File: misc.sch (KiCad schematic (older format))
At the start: 25 parts, among them CN8 POWER_INPUT, CN9 LED_CONNECTOR, SW1 POWER_SWITCH, SW2 RESET_SW, U10 NE555P, U11 74LS125, U12 74LS02, U9 74LS06

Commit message: Add buffers on joystick ports - WIP
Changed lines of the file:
@@
 Text Notes 6020 1880 0    50   ~ 0
 TCK-141
+$Comp
+L power:PWR_FLAG #FLG0103
+U 1 1 62290C11
+P 7000 1845
+F 0 "#FLG0103" H 7000 1920 50  0001 C CNN
+F 1 "PWR_FLAG" H 7000 2018 50  0000 C CNN
+F 2 "" H 7000 1845 50  0001 C CNN
+F 3 "~" H 7000 1845 50  0001 C CNN
+	1    7000 1845
+	1    0    0    -1
+$EndComp
+Wire Wire Line
+	7000 1845 7000 1945
 $EndSCHEMATC

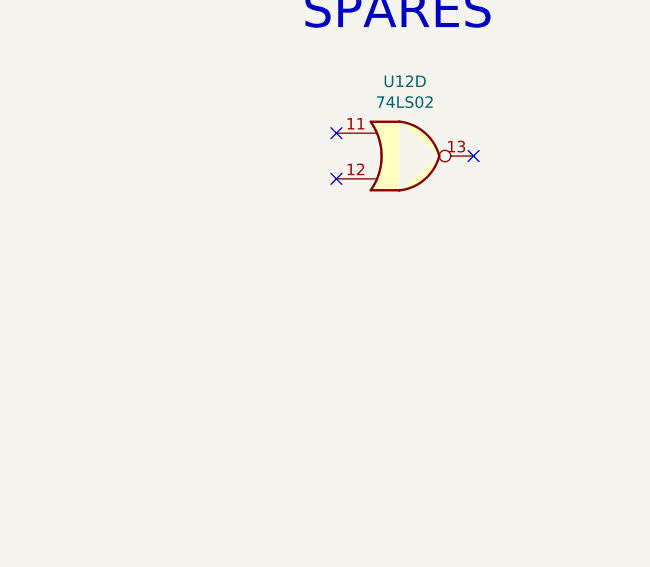
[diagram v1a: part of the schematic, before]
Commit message: Fit alt socket for 6510 Still some fine work TBD
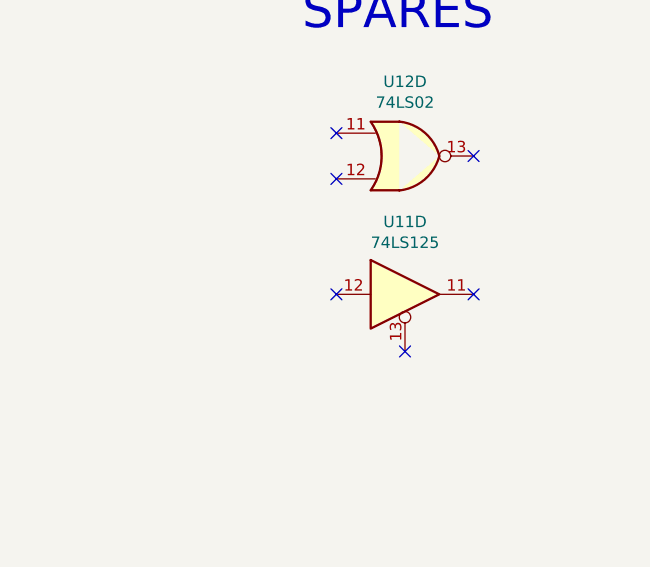
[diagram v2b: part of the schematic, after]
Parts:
- added unit 4 of U11
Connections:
- no-connect marks 5 -> 8
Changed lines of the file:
@@
 Wire Wire Line
 	7000 1845 7000 1945
+$Comp
+L 74xx:74LS125 U?
+U 4 1 625FE5B6
+P 9860 5960
+AR Path="/5ECB474B/625FE5B6" Ref="U?"  Part="4"
+AR Path="/5EACE220/625FE5B6" Ref="U11"  Part="4"
+F 0 "U11" H 9860 6277 50  0000 C CNN
+F 1 "74LS125" H 9860 6186 50  0000 C CNN
+F 2 "Package_DIP:DIP-14_W7.62mm_Socket_LongPads" H 9860 5960 50  0001 C CNN
+F 3 "http://www.ti.com/lit/gpn/sn74LS125" H 9860 5960 50  0001 C CNN
+	4    9860 5960
+	1    0    0    -1
+$EndComp
+NoConn ~ 9560 5960
+NoConn ~ 9860 6210
+NoConn ~ 10160 5960
 $EndSCHEMATC

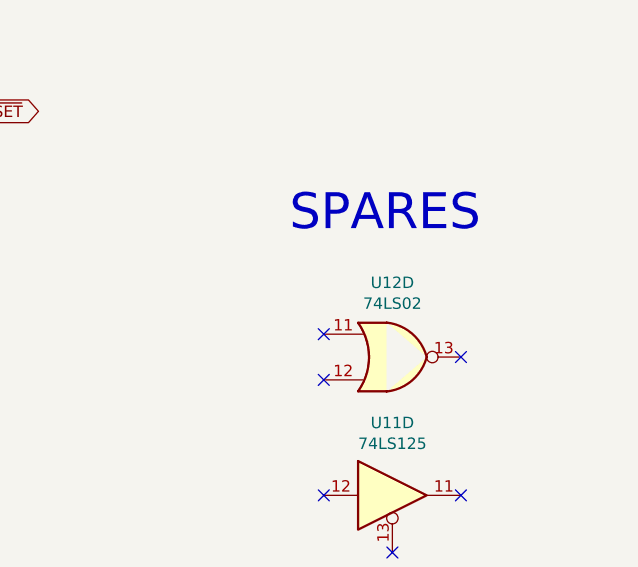
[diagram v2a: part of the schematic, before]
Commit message: Add a way to disable internal RAM from expansion connector
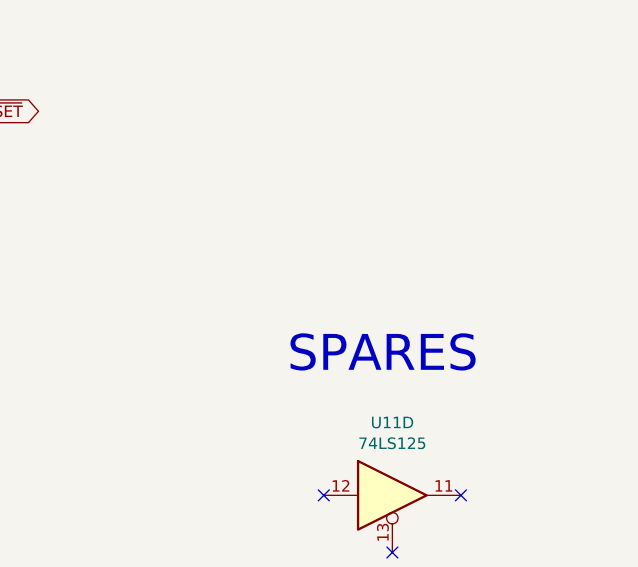
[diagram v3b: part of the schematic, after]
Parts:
- removed U12: 74LS02, Package_DIP:DIP-14_W7.62mm_Socket_LongPads, symbol 74xx:74LS02
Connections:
- no-connect marks 8 -> 5
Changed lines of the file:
@@
 Text Notes 1595 7490 0    50   ~ 0
 Additional\ndecoupling cap
-$Comp
-L 74xx:74LS02 U?
-U 4 1 6197C826
-P 9860 5355
-AR Path="/5EE7AAEB/6197C826" Ref="U?"  Part="4"
-AR Path="/5EACE220/6197C826" Ref="U12"  Part="4"
-F 0 "U12" H 9860 5680 50  0000 C CNN
-F 1 "74LS02" H 9860 5589 50  0000 C CNN
-F 2 "Package_DIP:DIP-14_W7.62mm_Socket_LongPads" H 9860 5355 50  0001 C CNN
-F 3 "http://www.ti.com/lit/gpn/sn74ls02" H 9860 5355 50  0001 C CNN
-	4    9860 5355
-	1    0    0    -1
-$EndComp
-NoConn ~ 9560 5255
-NoConn ~ 9560 5455
-NoConn ~ 10160 5355
-Text Notes 9410 4820 0    157  ~ 0
+Text Notes 9400 5440 0    157  ~ 0
 SPARES
 Text Notes 3130 3525 0    157  ~ 0

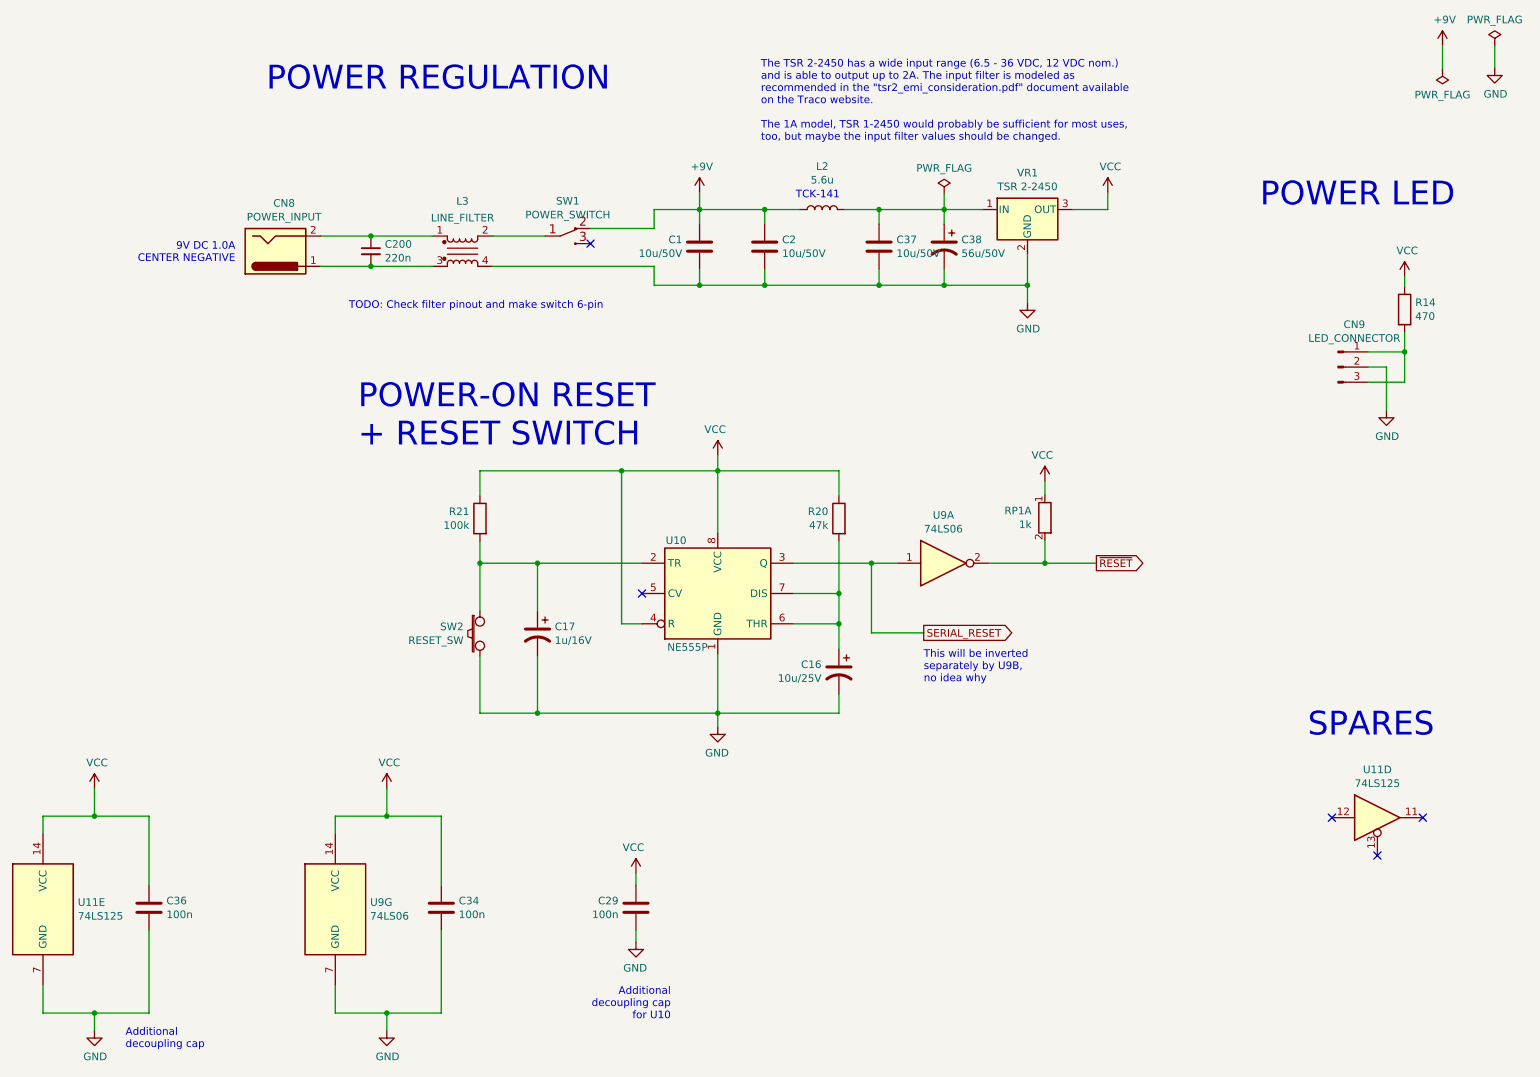
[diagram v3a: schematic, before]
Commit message: Rename extra caps and switch to full THT power circuit Well, there's one SMD component, but it's optional :)
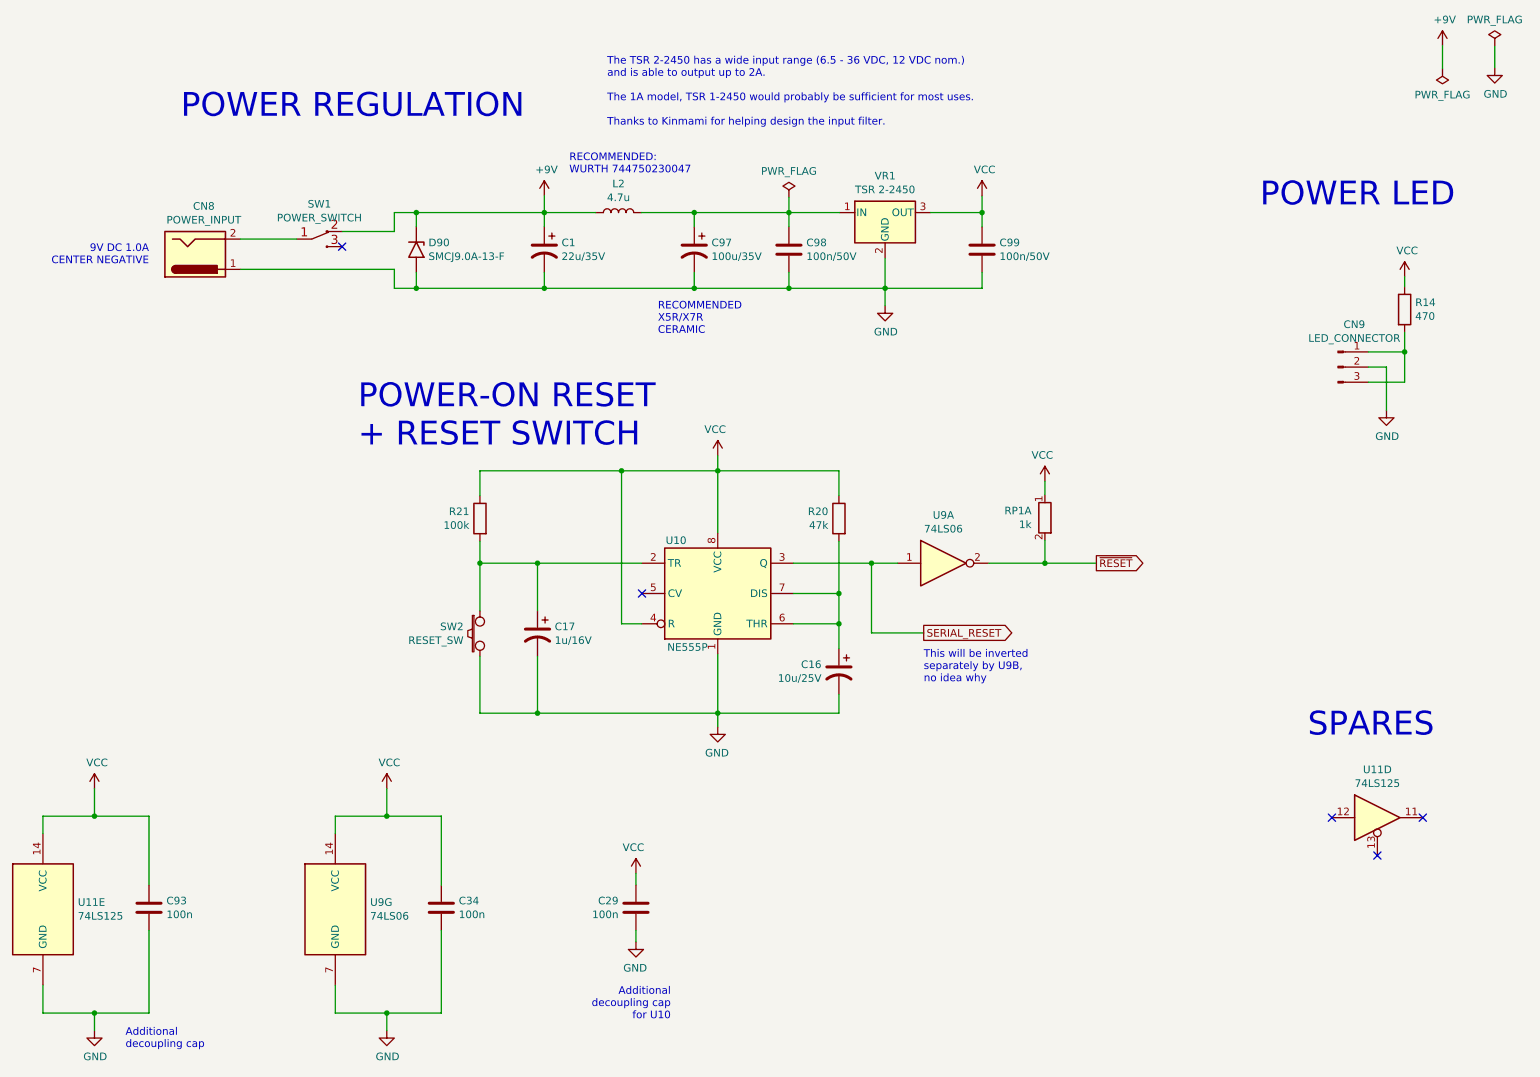
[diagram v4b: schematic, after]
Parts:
- removed C1, C2: 10u/50V, Capacitor_SMD:C_1206_3216Metric_Pad1.33x1.80mm_HandSolder, symbol Device:C
- removed C200: 220n, Capacitor_THT:C_Disc_D8.0mm_W2.5mm_P5.00mm, symbol Device:C_Small
- removed L3: LINE_FILTER, CommodorePlus4:Noise_Filter, symbol Device:EMI_Filter_LL
- added C1: 22u/35V, Capacitor_THT:CP_Radial_D8.0mm_P5.00mm, symbol Device:CP1
- added C99: 100n/50V, Capacitor_THT:C_Disc_D8.0mm_W2.5mm_P5.00mm, symbol Device:C
- added D90: SMCJ9.0A-13-F, Diode_SMD:D_SMC, symbol Diode:1.5KExxA
- C97: renamed from C38; value 56u/50V -> 100u/35V
- C98: renamed from C37; value 10u/50V -> 100n/50V; footprint Capacitor_SMD:C_1206_3216Metric_Pad1.33x1.80mm_HandSolder -> Capacitor_THT:C_Disc_D8.0mm_W2.5mm_P5.00mm
- L2: value 5.6u -> 4.7u; footprint Inductor_SMD:L_TracoPower_TCK-141 -> LittleSixteen:Inductor_Wurth_744750230047
- renumbered C36 to C93
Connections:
- net +9V: now also C1.1, D90.1 (A1)
- net GND: now also CN8.1, C1.2, C99.2, D90.2 (A2)
- net VCC: now also C99.1
- net at CN8.2: now also SW1.1 (COM)
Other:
- note added: "RECOMMENDED:\nWURTH 744750230047"
- note added: "RECOMMENDED\nX5R/X7R\nCERAMIC"
- note added: "The TSR 2-2450 has a wide input range (6.5 - 36 VDC, 12 VDC nom.)\nand is able to output up to 2A.\n\nThe 1A model, TSR 1-2450 would probably be sufficient for most uses.\n\nThanks to Kinmami for helping design the input filter."
- note removed: "TCK-141"
- note removed: "TODO: Check filter pinout and make switch 6-pin"
- note removed: "The TSR 2-2450 has a wide input range (6.5 - 36 VDC, 12 VDC nom.)\nand is able to output up to 2A. The input filter is modeled as\nrecommended in the "tsr2_emi_consideration.pdf" document available\non the Traco website.\n\nThe 1A model, TSR 1-2450 would probably be sufficient for most uses,\ntoo, but maybe the input filter values should be changed."
- moved on the sheet: C97, C98, CN8, L2, SW1, VR1

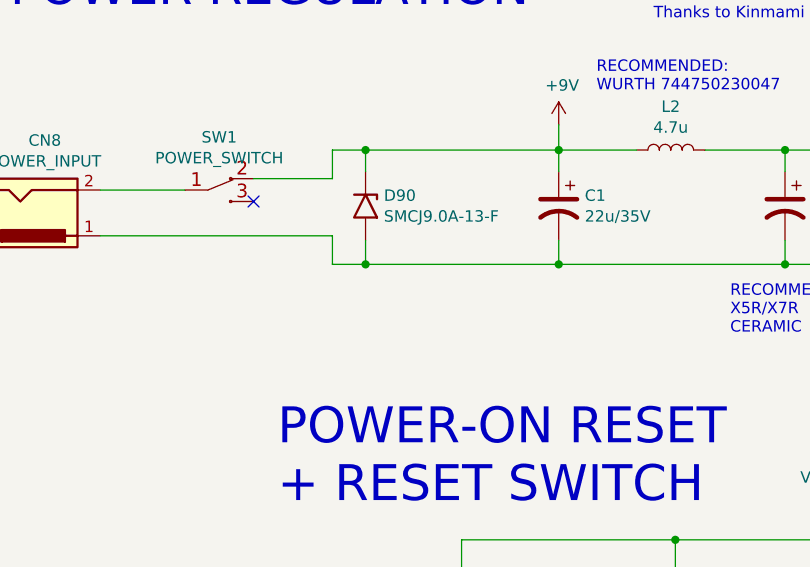
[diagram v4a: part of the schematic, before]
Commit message: Switch D90 to THT footprint
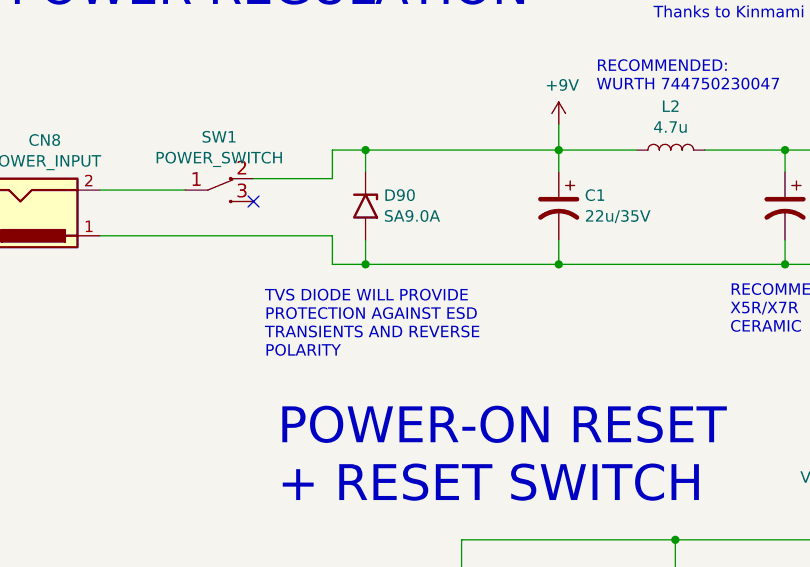
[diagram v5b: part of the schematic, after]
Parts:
- D90: value SMCJ9.0A-13-F -> SA9.0A; footprint Diode_SMD:D_SMC -> Diode_THT:D_DO-15_P5.08mm_Vertical_KathodeUp
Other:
- note added: "TVS DIODE WILL PROVIDE\nPROTECTION AGAINST ESD\nTRANSIENTS AND REVERSE\nPOLARITY"
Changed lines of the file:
@@
 Sheet 9 12
 Title "LittleSixteen"
-Date "2021-11-20"
+Date "2021-11-21"
 Rev "3git"
 Comp "SukkoPera"
@@
 P 3515 2210
 F 0 "D90" V 3469 2290 50  0000 L CNN
-F 1 "SMCJ9.0A-13-F" V 3560 2290 50  0000 L CNN
-F 2 "Diode_SMD:D_SMC" H 3515 2010 50  0001 C CNN
+F 1 "SA9.0A" V 3560 2290 50  0000 L CNN
+F 2 "Diode_THT:D_DO-15_P5.08mm_Vertical_KathodeUp" H 3515 2010 50  0001 C CNN
 F 3 "https://www.vishay.com/docs/88301/15ke.pdf" H 3465 2210 50  0001 C CNN
 	1    3515 2210
@@
 Wire Wire Line
 	3515 2465 4360 2465
+Text Notes 3075 2880 0    50   ~ 0
+TVS DIODE WILL PROVIDE\nPROTECTION AGAINST ESD\nTRANSIENTS AND REVERSE\nPOLARITY
 $EndSCHEMATC

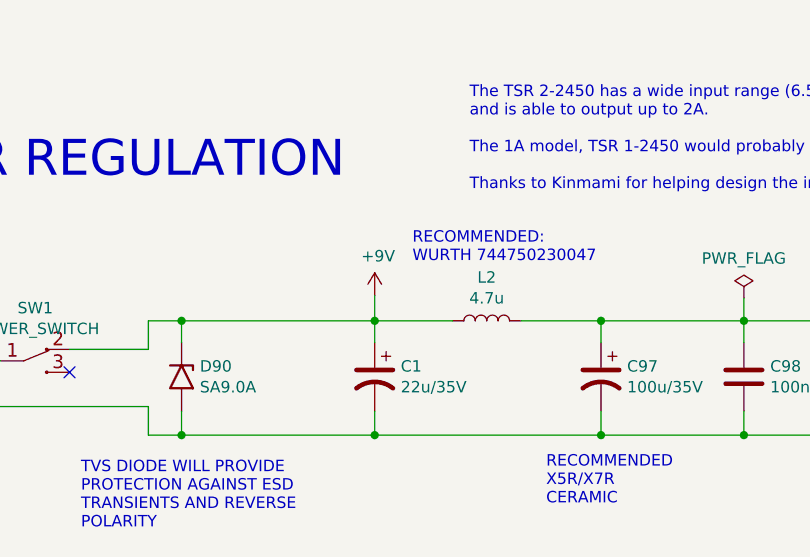
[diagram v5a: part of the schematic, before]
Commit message: Improve power zones
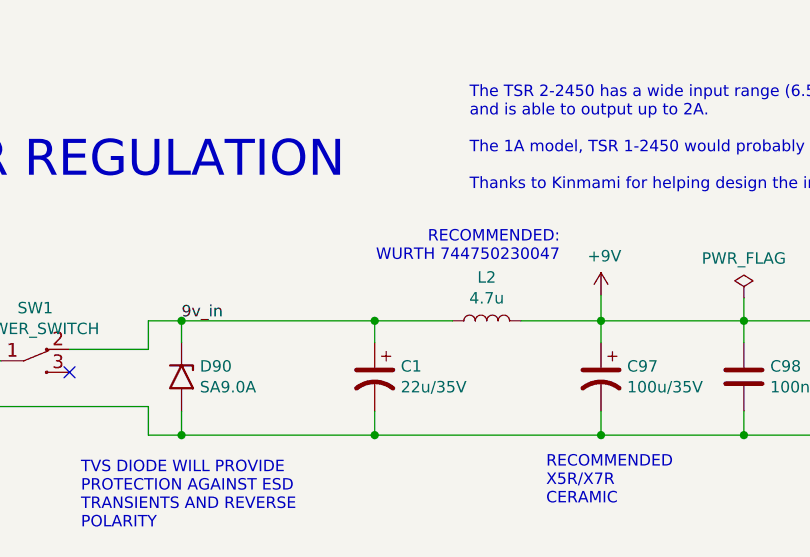
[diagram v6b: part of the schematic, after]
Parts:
- RP1: Notes (none) -> Bussed
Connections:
- net +9V: now also C97.1, C98.1, L2.2, VR1.1 (IN); no longer C1.1, D90.1 (A1), L2.1, SW1.2 (NC)
- new net 9v_in: C1.1, D90.1 (A1), L2.1, SW1.2 (NC)
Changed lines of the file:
@@
 Sheet 9 12
 Title "LittleSixteen"
-Date "2021-11-21"
+Date "2021-11-23"
 Rev "3git"
 Comp "SukkoPera"
@@
 F 2 "Resistor_THT:R_Array_SIP6" V 7595 3980 50  0001 C CNN
 F 3 "~" H 7665 3980 50  0001 C CNN
+F 4 "Bussed" H 7665 3980 50  0001 C CNN "Notes"
 	1    7665 3980
 	-1   0    0    -1
@@
 L power:+9V #PWR0149
 U 1 1 5ED51964
-P 4360 1855
-F 0 "#PWR0149" H 4360 1705 50  0001 C CNN
-F 1 "+9V" H 4375 2028 50  0000 C CNN
-F 2 "" H 4360 1855 50  0001 C CNN
-F 3 "" H 4360 1855 50  0001 C CNN
-	1    4360 1855
+P 5350 1855
+F 0 "#PWR0149" H 5350 1705 50  0001 C CNN
+F 1 "+9V" H 5365 2028 50  0000 C CNN
+F 2 "" H 5350 1855 50  0001 C CNN
+F 3 "" H 5350 1855 50  0001 C CNN
+	1    5350 1855
 	1    0    0    -1
 $EndComp
@@
 The TSR 2-2450 has a wide input range (6.5 - 36 VDC, 12 VDC nom.)\nand is able to output up to 2A.\n\nThe 1A model, TSR 1-2450 would probably be sufficient for most uses.\n\nThanks to Kinmami for helping design the input filter.
 Wire Wire Line
-	4360 1855 4360 1965
+	5350 1855 5350 1965
 Wire Wire Line
 	7250 1855 7250 1965
@@
 Wire Wire Line
 	6610 2465 7250 2465
-Text Notes 4525 1715 0    50   ~ 0
+Text Notes 5170 1710 2    50   ~ 0
 RECOMMENDED:\nWURTH 744750230047
 $Comp
@@
 Text Notes 3075 2880 0    50   ~ 0
 TVS DIODE WILL PROVIDE\nPROTECTION AGAINST ESD\nTRANSIENTS AND REVERSE\nPOLARITY
+Text Label 3515 1965 0    50   ~ 0
+9v_in
 $EndSCHEMATC
